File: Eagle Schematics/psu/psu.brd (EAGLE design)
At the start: 160 x 100 mm, 14 parts, among them IC1 7805T, IC2 7805T, IC3 REG1117

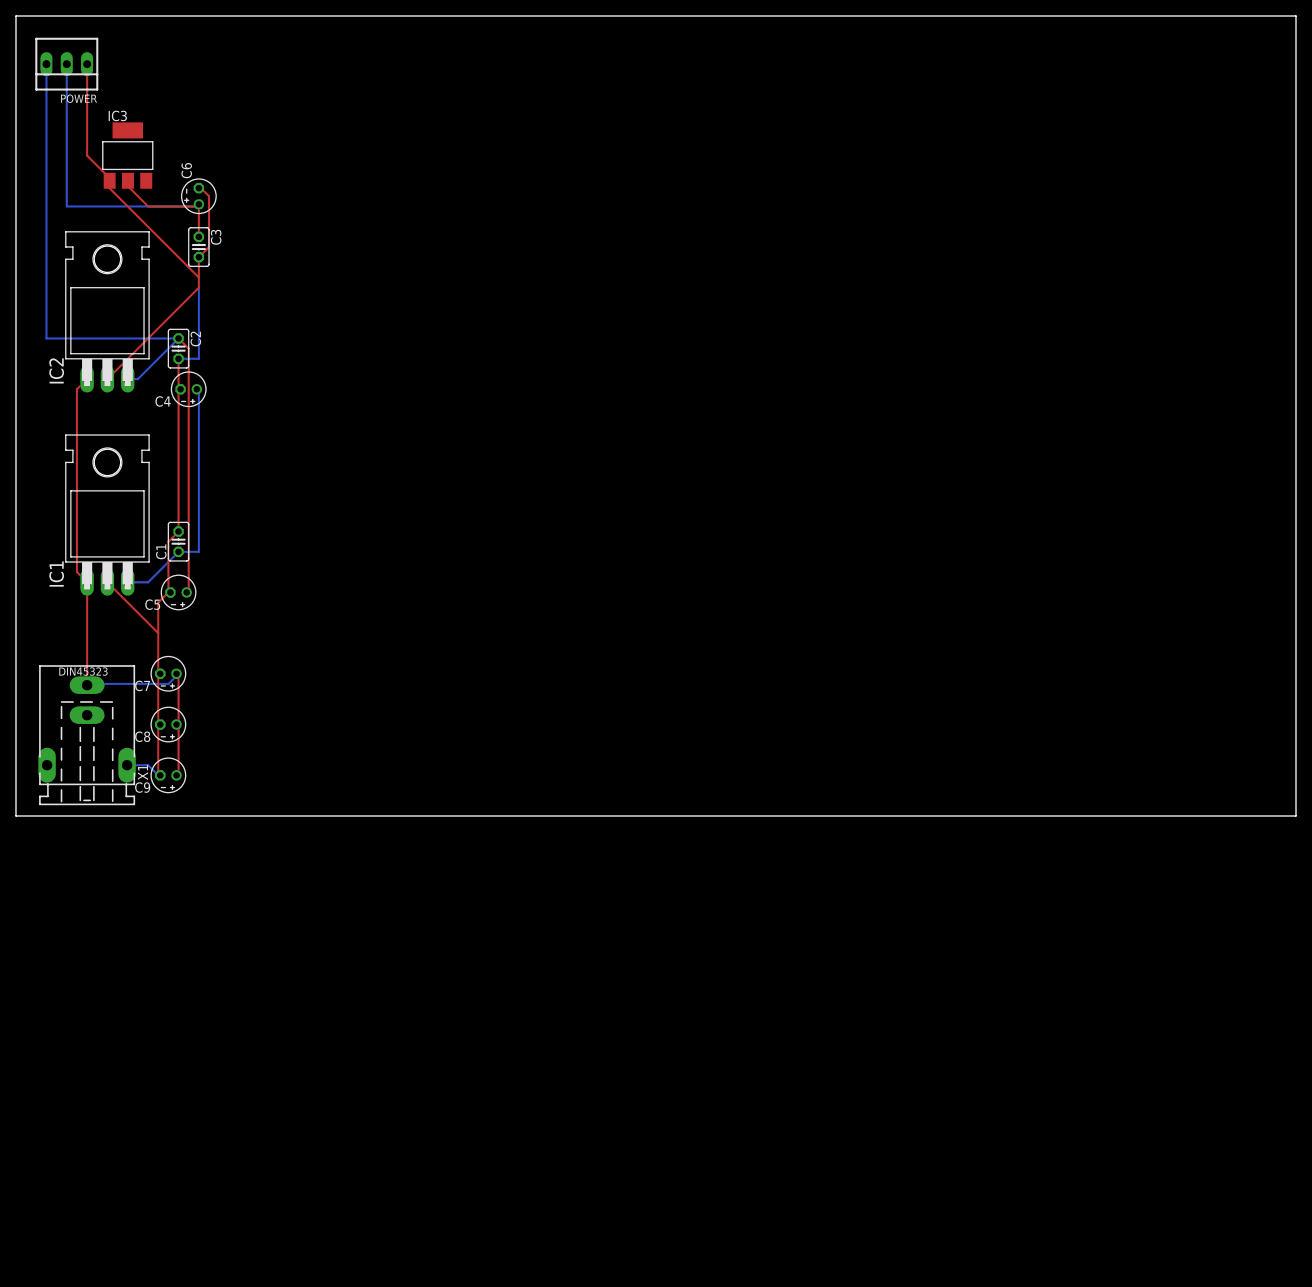
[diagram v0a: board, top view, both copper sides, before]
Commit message: Added PSU and entity module schematic
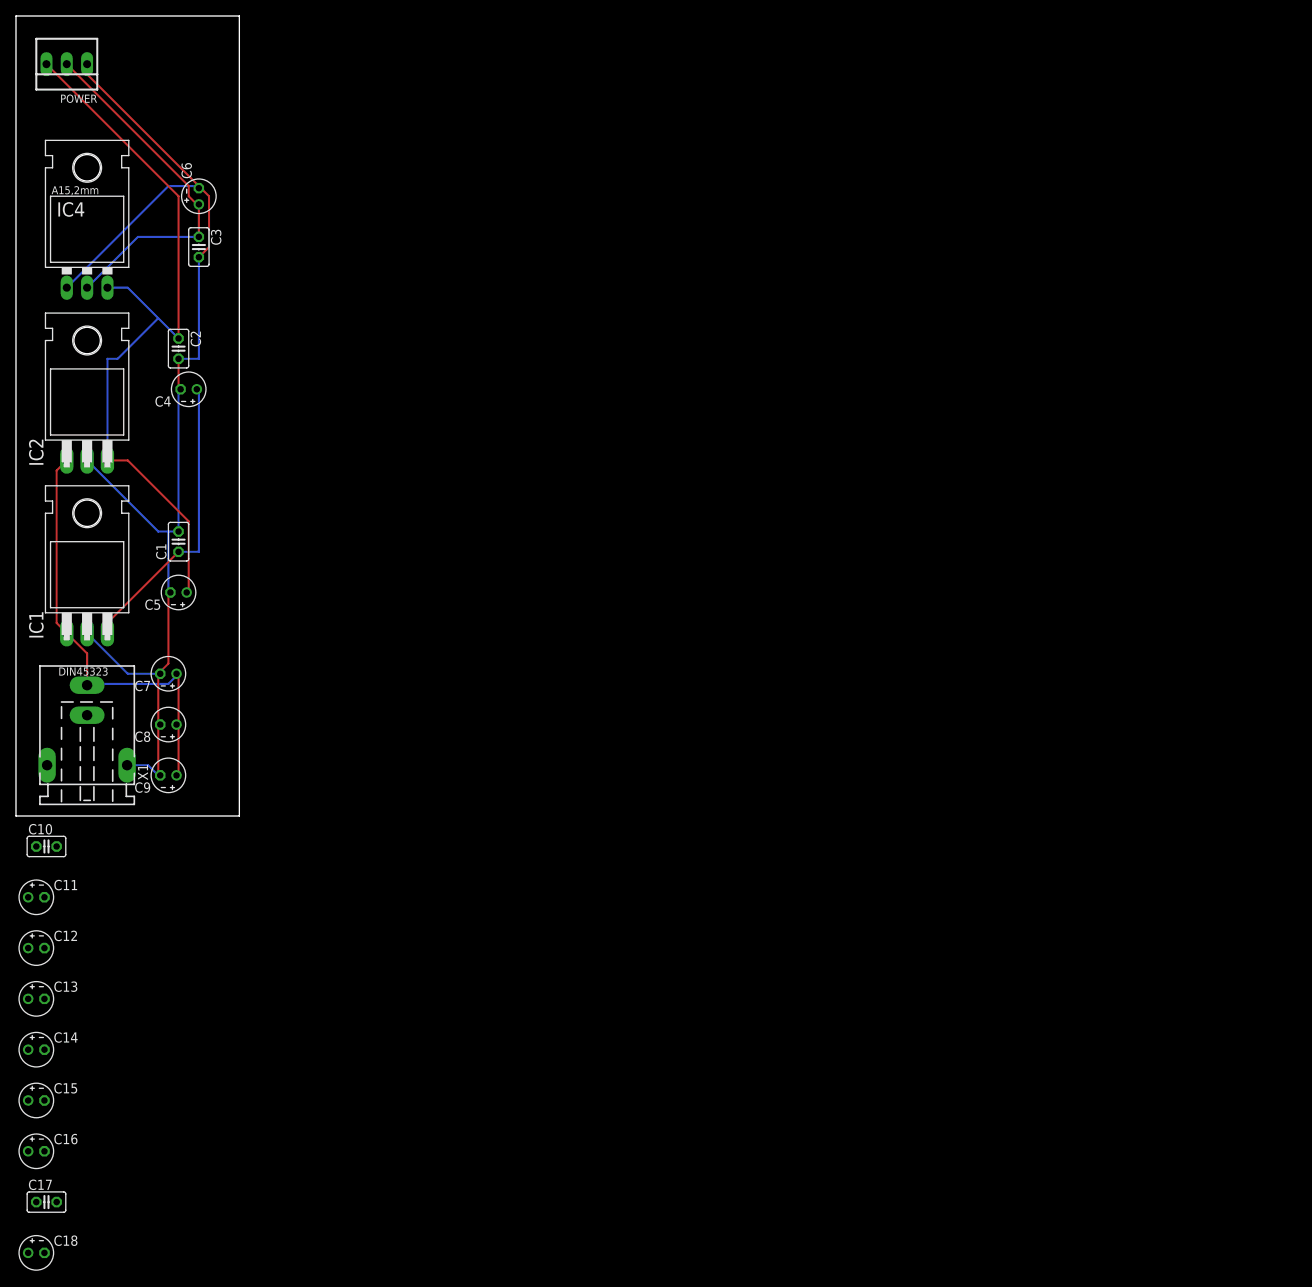
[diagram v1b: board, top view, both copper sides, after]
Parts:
- removed IC3: REG1117, burr-brown:SOT223
- added C10, C17: 0.1uF, rcl:C025-025X050
- added C11, C18: 100uF, rcl:E2-4
- added C12, C13, C14, C15, C16: 470uF, rcl:E2-4
- added IC4: LD117AV33, v-reg:TO220L1
- moved IC2 10.5 mm to (8.89, 54.6)
- moved IC1 6.84 mm to (8.89, 33.0)
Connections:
- net BB-5V: now also C13.+
- net GND: now also C10.2, C11.-, C12.-, C13.-, C14.-, C15.-, C16.-, C17.2, C18.-, IC4.1; no longer IC3.1
- net N$1: now also C14.+, C16.+, C17.1, C18.+, IC4.3
- net N$3: now also C15.+, IC4.2; no longer IC3.2
- net VCC: now also C10.1, C11.+, C12.+
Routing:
- net VCC: track 65.1 -> 56.0 mm
- net GND: track 146.0 -> 153.9 mm
- net BB-5V: track 31.0 -> 37.0 mm
- net N$1: track 91.8 -> 96.3 mm
- net N$3: track 49.2 -> 45.3 mm
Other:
- board size 160 x 100 mm -> 27.9 x 100 mm

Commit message: Updated PSU schematic and documentation
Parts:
- removed C10: 0.1uF, rcl:C025-025X050
- removed C11, C18, C6: 100uF, rcl:E2-4
- removed C12, C13, C14, C15: 470uF, rcl:E2-4
- removed X1: (no value), con-conrad:737992-5
- added BEAGLEBONE, EM, EM1, MOTORS, MOTORS1: (no value), con-amp-quick:02P
- added D1, D10, D2, D3, D4, D8, D9: 1N4007, diode:DO41-10
- added F1: FUSE 1A, fuse:PICOFUSE
- added F5: FUSE 4.5A, fuse:PICOFUSE
- added IC10: 7805T, linear:TO220H
- added IC3, IC5: 7812T, linear:TO220H
- added UPCB-POWER: 22-23-2031, con-molex:22-23-2031
- C16: value 470uF -> 0.1uF; device rcl:E2-4 -> rcl:C025-025X050
- C4: value 100uF -> 47000uF; device rcl:E2-4 -> rcl:E2,5-6E
- C5: value 100uF -> 4700uF; device rcl:E2-4 -> rcl:E2,5-6E
- C7: value 2F -> 0.33uF; device rcl:E2-4 -> rcl:C025-025X050
- C8: value 1F -> 0.33uF; device rcl:E2-4 -> rcl:C025-025X050
- C9: value 0.5F -> 4700uF; device rcl:E2-4 -> rcl:E2,5-6E
- POWER: value 22-23-2031 -> (none); device con-molex:22-23-2031 -> con-amp-quick:02P
- moved POWER 407.8 mm to (-148.6, -283.2), turned to 0 degrees
- moved C9 377.2 mm to (-156.2, -328.9), turned to 0 degrees
- moved C1 310.2 mm to (-111.8, -246.4), turned to 0 degrees
- moved C17 209.9 mm to (-111.8, -223.5)
- moved C16 208.2 mm to (-111.8, -215.9)
- moved C5 183.3 mm to (-95.2, -114.3), turned to 0 degrees
- moved C4 156.2 mm to (-12.7, -99.1), turned to 0 degrees
- moved C8 107.7 mm to (-12.7, -91.4), turned to 0 degrees
- moved C7 106.4 mm to (-12.7, -83.8), turned to 0 degrees
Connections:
- removed net BB-5V: C1.1, C13.+, C4.+, IC1.3
- removed net N$1: C14.+, C16.+, C17.1, C18.+, C2.1, C5.+, IC2.3, IC4.3, POWER.3
- new net 12V: C5.+, D2.A, IC3.3
- new net 12V1: C9.+, D4.A, IC5.3
- new net 3.3V: C3.1, IC4.2, UPCB-POWER.2
- new net 5-1A,1: C16.1, D9.A, IC1.3
- new net 5V: C2.1, C8.1, IC2.3, IC4.3, UPCB-POWER.3
- new net 5V-1A,2: C17.1, D10.A, IC10.3
- new net BB-POWER: BEAGLEBONE.2, D10.C, D9.C
- new net EM-POWER: D2.C, F1.1
- new net GND-IC1: D3.A, IC5.2
- new net GND-IC1,10: D8.A, IC1.2, IC10.2
- new net GND-IC3: D1.A, IC3.2
- new net KINECT-POWER: D4.C, EM1.2
- new net N$2: F5.2, MOTORS.2, MOTORS1.2
- new net VCC1: IC5.1
- net GND: now also BEAGLEBONE.1, C16.2, C7.2, C8.2, D1.C, D3.C, D8.C, EM.1, EM1.1, MOTORS.1, MOTORS1.1, UPCB-POWER.1; no longer C10.2, C11.-, C12.-, C13.-, C14.-, C15.-, C16.-, C18.-, C6.-, C7.-, C8.-, IC1.2, X1.-1
- net N$3: now also EM.2, F1.2; no longer C15.+, C3.1, C6.+, IC4.2, POWER.2
- net VCC: now also C1.1, C4.+, C7.1, F5.1, IC10.1, IC3.1, POWER.2; no longer C10.1, C11.+, C12.+, C7.+, C8.+, C9.+, X1.+
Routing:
- net N$1: track 96.3 -> 0.00 mm
- net GND: track 153.9 -> 93.3 mm
- net N$3: track 45.3 -> 0.00 mm
- net 5V: track 0.00 -> 37.8 mm
- net BB-5V: track 37.0 -> 0.00 mm
- net VCC: track 56.0 -> 20.8 mm
- net 3.3V: track 0.00 -> 23.5 mm

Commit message: Finalized PSU schematic
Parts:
- removed EM1: (no value), con-amp-quick:02P
- added KINECT: (no value), con-amp-quick:02P
- moved D3 391.2 mm to (45.7, 22.9), turned to 90 degrees
- moved C9 387.5 mm to (38.1, 6.35)
- moved IC5 378.7 mm to (33.0, 33.0)
- moved D4 376.5 mm to (44.5, 14.0), turned to 180 degrees
- moved MOTORS1 365.6 mm to (67.3, 5.08)
- moved F1 354.6 mm to (58.4, 58.4), turned to 180 degrees
- moved F5 349.1 mm to (69.8, 15.2)
- moved BEAGLEBONE 344.8 mm to (49.5, 5.08)
- moved MOTORS 340.0 mm to (58.4, 5.08)
- moved POWER 326.7 mm to (5.08, 5.08)
- moved EM 322.6 mm to (14.0, 5.08)
- moved C1 321.8 mm to (45.7, 34.3)
- moved D10 306.1 mm to (55.9, 19.1), turned to 180 degrees
- moved IC10 302.2 mm to (31.8, 85.1)
- moved C17 295.9 mm to (21.6, 40.6)
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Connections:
- net GND: now also KINECT.1; no longer EM1.1
- net KINECT-POWER: now also KINECT.2; no longer EM1.2
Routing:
- net GND: track 93.3 -> 307.6 mm
- net VCC: track 20.8 -> 154.9 mm
- net 5V-1A,2: track 0.00 -> 95.0 mm
- net N$3: track 0.00 -> 86.8 mm
- net GND-IC1,10: track 0.00 -> 77.2 mm
- net BB-POWER: track 0.00 -> 62.7 mm
- net 5V: track 37.8 -> 72.7 mm
- net N$2: track 0.00 -> 32.2 mm
- net KINECT-POWER: track 0.00 -> 29.1 mm
- net 3.3V: track 23.5 -> 48.7 mm
- net 12V: track 0.00 -> 19.6 mm
- net 12V1: track 0.00 -> 19.1 mm
- net GND-IC1: track 0.00 -> 14.8 mm
- net 5-1A,1: track 0.00 -> 14.5 mm
- net EM-POWER: track 0.00 -> 13.8 mm
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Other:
- board size 27.9 x 100 mm -> 80 x 100 mm
